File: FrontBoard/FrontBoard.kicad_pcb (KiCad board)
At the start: 2 copper layers, 20.3 x 113.1 mm, 17 parts

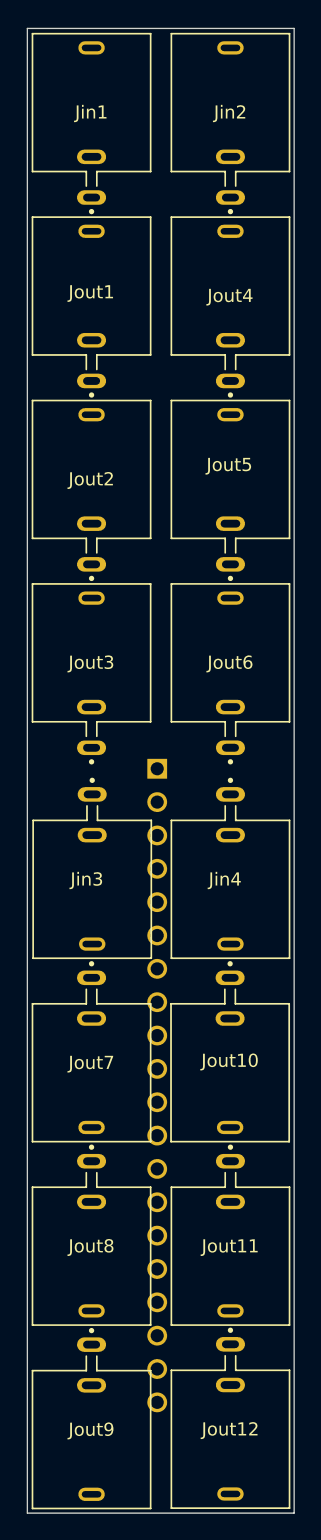
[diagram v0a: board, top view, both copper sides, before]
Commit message: updated with new footprints and 3d models
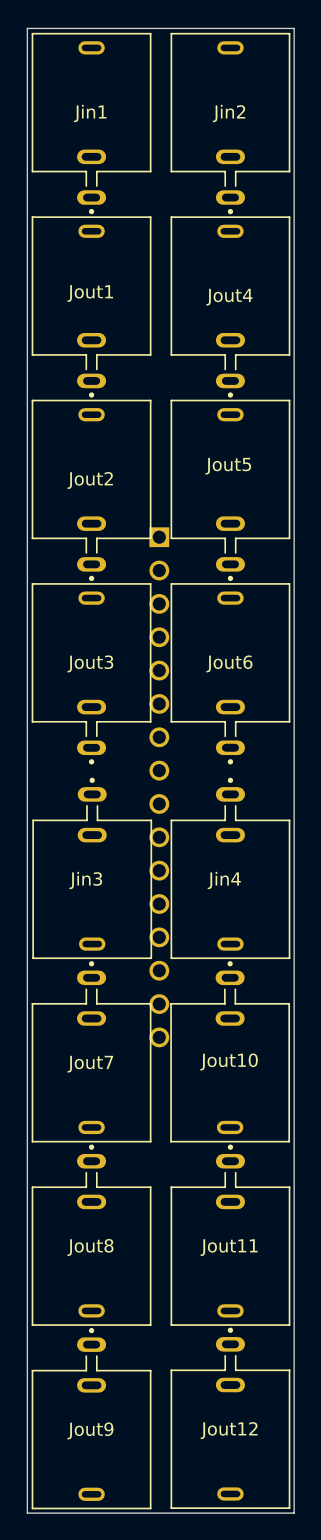
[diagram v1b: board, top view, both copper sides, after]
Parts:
- Jheader1: footprint 2-826646-0:TE_2-826646-0 -> TE_1-826936-6:TE_1-826936-6
- moved Jheader1 22.7 mm to (162.4, 97.1)
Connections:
- Jin1 pad 1: GNDPWR -> GND
- Jin1 pad 2: GNDPWR -> GND
- Jin2 pad 1: GNDPWR -> GND
- Jin3 pad 1: GNDPWR -> GND
- Jin4 pad 1: GNDPWR -> GND
- Jout1 pad 1: GNDPWR -> GND
- Jout1 pad 2: GNDPWR -> GND
- Jout10 pad 1: GNDPWR -> GND
- Jout10 pad 2: GNDPWR -> GND
- Jout10 pad 3: Output10 -> Output8
- Jout11 pad 1: GNDPWR -> GND
- Jout11 pad 2: GNDPWR -> GND
- Jout11 pad 3: Output11 -> Output9
- Jout12 pad 1: GNDPWR -> GND
- Jout12 pad 2: GNDPWR -> GND
- Jout12 pad 3: Output12 -> Output10
- Jout2 pad 1: GNDPWR -> GND
- Jout2 pad 2: GNDPWR -> GND
- Jout3 pad 1: GNDPWR -> GND
- Jout3 pad 2: GNDPWR -> GND
- Jout5 pad 1: GNDPWR -> GND
- Jout5 pad 2: GNDPWR -> GND
- Jout5 pad 3: Output5 -> Output4
- Jout6 pad 1: GNDPWR -> GND
- Jout6 pad 2: GNDPWR -> GND
- Jout6 pad 3: Output6 -> Output5
- Jout7 pad 1: GNDPWR -> GND
- Jout7 pad 2: GNDPWR -> GND
- Jout7 pad 3: Output7 -> Output6
- Jout9 pad 1: GNDPWR -> GND
- Jout9 pad 2: GNDPWR -> GND
- Jout9 pad 3: Output9 -> Output7

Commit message: updated placement
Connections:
- Jheader1 pad 12: Output8 -> Output5
- Jheader1 pad 13: Output9 -> Output8
- Jheader1 pad 14: Output10 -> Output6
- Jheader1 pad 7: Output5 -> Output9
- Jheader1 pad 8: Output6 -> Output10
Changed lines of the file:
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@@
   (footprint "TE_1-826936-6:TE_1-826936-6" (layer "B.Cu")
     (at 162.45 97.12 -90)
-    (property "Comment" "2-826646-0")
+    (property "Centerline_Pitch" "2.54 mm[.1 in]")
+    (property "Comment" "1-826936-6")
     (property "EU_RoHS_Compliance" "Compliant")
+    (property "Number_of_Positions" "16")
+    (property "Product_Type" "Connector")
     (property "Sheetfile" "FrontBoard.kicad_sch")
     (property "Sheetname" "")
+    (property "Sim.Device" "SPICE")
+    (property "Sim.Enable" "0")
+    (property "Sim.Params" "type=\"J\" model=\"2-826646-0\" lib=\"\"")
+    (property "Sim.Pins" "1=1 2=2 3=3 4=4 5=5 6=6 7=7 8=8 9=9 10=10 11=11 12=12 13=13 14=14 15=15 16=16 17=17 18=18 19=19 20=20")
     (attr through_hole)
     (fp_text reference "Jheader1" (at -18.145 2.885 90) (layer "B.SilkS")
@@
       (net 6 "Output4") (pinfunction "6") (pintype "passive"))
     (pad "7" thru_hole circle (at -3.81 0 270) (size 1.508 1.508) (drill 1) (layers "*.Cu" "*.Mask")
-      (net 7 "Output5") (pinfunction "7") (pintype "passive"))
+      (net 12 "Output9") (pinfunction "7") (pintype "passive"))
     (pad "8" thru_hole circle (at -1.27 0 270) (size 1.508 1.508) (drill 1) (layers "*.Cu" "*.Mask")
-      (net 8 "Output6") (pinfunction "8") (pintype "passive"))
+      (net 13 "Output10") (pinfunction "8") (pintype "passive"))
     (pad "9" thru_hole circle (at 1.27 0 270) (size 1.508 1.508) (drill 1) (layers "*.Cu" "*.Mask")
       (net 16 "InputBus3") (pinfunction "9") (pintype "passive"))
@@
       (net 9 "Output7") (pinfunction "11") (pintype "passive"))
     (pad "12" thru_hole circle (at 8.89 0 270) (size 1.508 1.508) (drill 1) (layers "*.Cu" "*.Mask")
-      (net 10 "Output8") (pinfunction "12") (pintype "passive"))
+      (net 7 "Output5") (pinfunction "12") (pintype "passive"))
     (pad "13" thru_hole circle (at 11.43 0 270) (size 1.508 1.508) (drill 1) (layers "*.Cu" "*.Mask")
-      (net 12 "Output9") (pinfunction "13") (pintype "passive"))
+      (net 10 "Output8") (pinfunction "13") (pintype "passive"))
     (pad "14" thru_hole circle (at 13.97 0 270) (size 1.508 1.508) (drill 1) (layers "*.Cu" "*.Mask")
-      (net 13 "Output10") (pinfunction "14") (pintype "passive"))
+      (net 8 "Output6") (pinfunction "14") (pintype "passive"))
     (pad "15" thru_hole circle (at 16.51 0 270) (size 1.508 1.508) (drill 1) (layers "*.Cu" "*.Mask")
       (net 14 "Output11") (pinfunction "15") (pintype "passive"))

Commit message: first pass at routing mainboard
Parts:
- Jheader1: footprint TE_1-826936-6:TE_1-826936-6 -> ESQ-120-12-T-S:SAMTEC_ESQ-120-12-T-S
- moved Jheader1 35.0 mm to (162.5, 62.1)
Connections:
- Jout10 pad 3: Output8 -> Output10
- Jout11 pad 3: Output9 -> Output11
- Jout12 pad 3: Output10 -> Output12
- Jout4 pad 1: GNDPWR -> GND
- Jout4 pad 2: GNDPWR -> GND
- Jout5 pad 3: Output4 -> Output5
- Jout6 pad 3: Output5 -> Output6
- Jout7 pad 3: Output6 -> Output7
- Jout8 pad 1: GNDPWR -> GND
- Jout8 pad 2: GNDPWR -> GND
- Jout9 pad 3: Output7 -> Output9

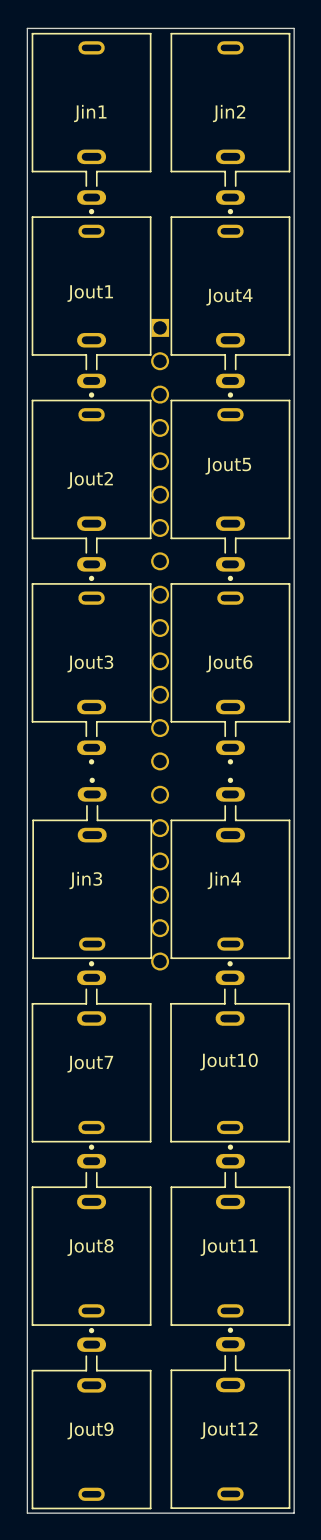
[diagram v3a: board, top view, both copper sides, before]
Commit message: converted MainBoard to 4 layer stackup
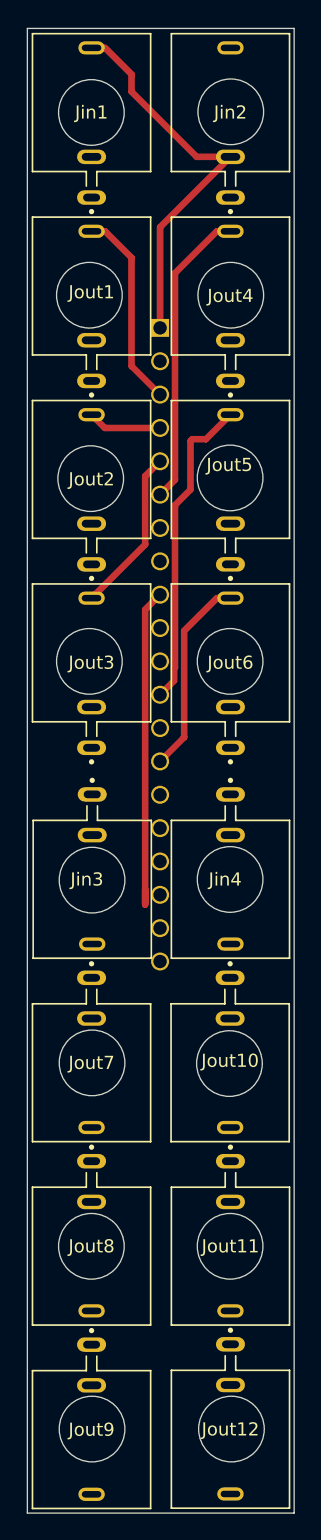
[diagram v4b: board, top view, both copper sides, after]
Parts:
- added REF**: MountingHole_5mm, MountingHole:MountingHole_5mm, B.Cu at (167.8, 118.2)
- added REF**: MountingHole_5mm, MountingHole:MountingHole_5mm, B.Cu at (157.3, 146.0)
- added REF**: MountingHole_5mm, MountingHole:MountingHole_5mm, B.Cu at (157.1, 87.5)
- added REF**: MountingHole_5mm, MountingHole:MountingHole_5mm, B.Cu at (157.3, 132.1)
- added REF**: MountingHole_5mm, MountingHole:MountingHole_5mm, B.Cu at (167.8, 87.5)
- added REF**: MountingHole_5mm, MountingHole:MountingHole_5mm, B.Cu at (167.8, 104.1)
- added REF**: MountingHole_5mm, MountingHole:MountingHole_5mm, B.Cu at (157.2, 73.6)
- added REF**: MountingHole_5mm, MountingHole:MountingHole_5mm, B.Cu at (167.9, 146.0)
- added REF**: MountingHole_5mm, MountingHole:MountingHole_5mm, B.Cu at (157.3, 104.2)
- added REF**: MountingHole_5mm, MountingHole:MountingHole_5mm, B.Cu at (167.9, 45.7)
- added REF**: MountingHole_5mm, MountingHole:MountingHole_5mm, B.Cu at (157.3, 118.1)
- added REF**: MountingHole_5mm, MountingHole:MountingHole_5mm, B.Cu at (167.8, 73.6)
- added REF**: MountingHole_5mm, MountingHole:MountingHole_5mm, B.Cu at (157.3, 45.7)
- added REF**: MountingHole_5mm, MountingHole:MountingHole_5mm, B.Cu at (167.8, 132.1)
- added REF**: MountingHole_5mm, MountingHole:MountingHole_5mm, B.Cu at (167.9, 59.6)
- added REF**: MountingHole_5mm, MountingHole:MountingHole_5mm, B.Cu at (157.1, 59.6)
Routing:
- net InputBus1: track 0.00 -> 30.0 mm
- net InputBus3: track 0.00 -> 25.3 mm
- net Output5: track 0.00 -> 24.2 mm
- net Output4: track 0.00 -> 22.9 mm
- net Output6: track 0.00 -> 15.3 mm
- net Output1: track 0.00 -> 15.2 mm
- net Output3: track 0.00 -> 12.6 mm
- net Output2: track 0.00 -> 5.64 mm

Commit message: WIP: added faceplate
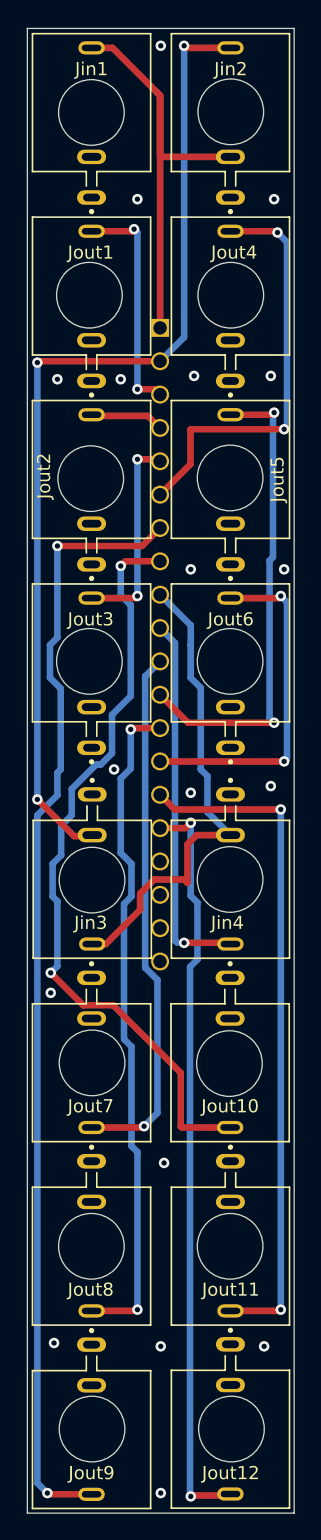
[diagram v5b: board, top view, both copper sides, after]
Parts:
- renumbered REF** to Jinhole1, REF** to Jinhole2, REF** to Jinhole3, REF** to Jinhole4, REF** to Jouthole1, REF** to Jouthole11, REF** to Jouthole3, REF** to Jouthole4, REF** to Jouthole5, REF** to Jouthole7, REF** to Jouthole9, REF** to jouthole10, REF** to jouthole12, REF** to jouthole2, REF** to jouthole6, REF** to jouthole8
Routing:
- net Output9: track 0.00 -> 85.6 mm, vias 0 -> 2
- net InputBus2: track 0.00 -> 76.4 mm, vias 0 -> 3
- net Output10: track 0.00 -> 58.4 mm, vias 0 -> 2
- net Output12: track 0.00 -> 57.4 mm, vias 0 -> 2
- net Output11: track 0.00 -> 51.6 mm, vias 0 -> 2
- net Output8: track 0.00 -> 51.3 mm, vias 0 -> 2
- net Output7: track 0.00 -> 40.7 mm, vias 0 -> 1
- net InputBus4: track 0.00 -> 28.2 mm, vias 0 -> 1
- net Output5: track 24.2 -> 36.9 mm, vias 0 -> 2
- net InputBus3: track 25.3 -> 37.1 mm
- net Output6: track 15.3 -> 25.9 mm, vias 0 -> 2
- net Output4: track 22.9 -> 32.1 mm, vias 0 -> 2
- net InputBus1: track 30.0 -> 34.5 mm
- net Output3: track 12.6 -> 15.8 mm, vias 0 -> 2
- net Output1: track 15.2 -> 17.5 mm, vias 0 -> 2
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- added copper zone on In1.Cu, net GND
- added copper zone on In2.Cu, net GND
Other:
- copper layers 2 -> 4

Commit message: sent to production v1.0.0
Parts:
- moved Jouthole3 0.19 mm to (157.3, 87.6), turned to 0 degrees
- moved Jouthole1 0.17 mm to (157.3, 59.7)
- moved Jouthole5 0.10 mm to (167.9, 73.7)
- moved jouthole6 0.10 mm to (167.9, 87.6), turned to 0 degrees
- moved jouthole2 0.08 mm to (157.3, 73.7), turned to 0 degrees
- moved jouthole12 0.08 mm to (167.9, 146.0)
- moved jouthole10 0.07 mm to (167.8, 118.1)
- moved Jinhole2 0.06 mm to (167.9, 45.7), turned to 0 degrees
- moved Jouthole4 0.06 mm to (167.9, 59.7), turned to 0 degrees
- moved Jinhole3 0.05 mm to (157.3, 104.1)
- turned Jinhole1 to 0 degrees
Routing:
- net Output5: track 36.9 -> 37.5 mm
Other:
- board text added: "R-mods v1.0.0 2023"

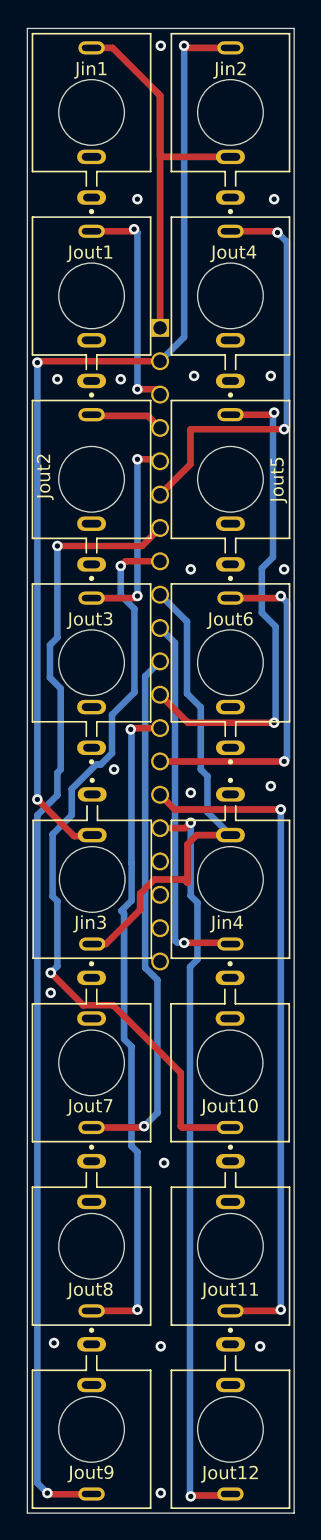
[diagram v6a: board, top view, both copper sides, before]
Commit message: fixed incorrect routing on Jheader1, moved silk screens to back layer for easy readability after assembly, oriented all jacks in the upright postition to solvealignnment descrepency in 3d model vs gerber print
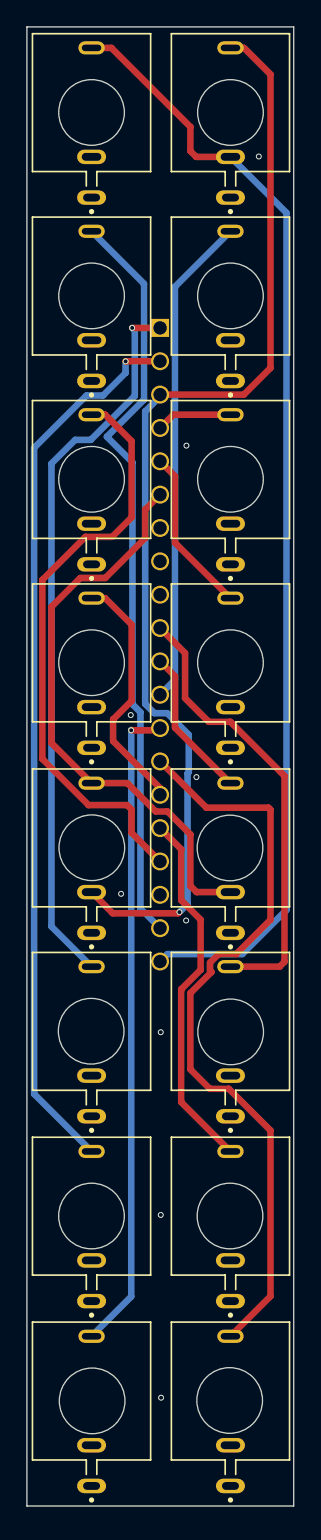
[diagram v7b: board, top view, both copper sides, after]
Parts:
- moved Jin3 2.42 mm to (157.3, 101.7), turned to 0 degrees
- moved Jinhole3 2.42 mm to (157.3, 101.7)
- moved Jin4 2.42 mm to (167.9, 101.7), turned to 0 degrees
- moved Jouthole7 2.41 mm to (157.3, 115.7)
- moved Jout10 2.41 mm to (167.9, 115.7), turned to 0 degrees
- moved Jout7 2.41 mm to (157.3, 115.7), turned to 0 degrees
- moved Jinhole4 2.40 mm to (167.8, 101.7)
- moved jouthole10 2.36 mm to (167.9, 115.7), turned to 0 degrees
- moved Jouthole11 2.31 mm to (167.8, 129.8), turned to 0 degrees
- moved jouthole8 2.31 mm to (157.3, 129.8), turned to 0 degrees
- moved Jout11 2.31 mm to (167.9, 129.8), turned to 0 degrees
- moved Jout8 2.31 mm to (157.3, 129.8), turned to 0 degrees
- moved jouthole12 2.20 mm to (167.8, 143.8), turned to 0 degrees
- moved Jouthole9 2.17 mm to (157.3, 143.9), turned to 0 degrees
- moved Jout12 2.17 mm to (167.9, 143.9), turned to 0 degrees
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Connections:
- Jheader1 pad 01: InputBus1 -> Output7
- Jheader1 pad 02: InputBus2 -> Output8
- Jheader1 pad 03: Output1 -> InputBus2
- Jheader1 pad 04: Output2 -> Output5
- Jheader1 pad 05: Output3 -> Output6
- Jheader1 pad 06: Output4 -> InputBus3
- Jheader1 pad 07: Output9 -> GND
- Jheader1 pad 08: Output10 -> GND
- Jheader1 pad 09: InputBus3 -> GND
- Jheader1 pad 10: InputBus4 -> Output10
- Jheader1 pad 11: Output7 -> InputBus4
- Jheader1 pad 12: Output5 -> Output4
- Jheader1 pad 13: Output8 -> Output9
- Jheader1 pad 14: Output6 -> Output12
- Jheader1 pad 15: Output11 -> Output3
- Jheader1 pad 16: Output12 -> Output11
- Jheader1 pad 17: GND -> Output2
- Jheader1 pad 19: GND -> Output1
- Jheader1 pad 20: GND -> InputBus1
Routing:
- net InputBus1: track 34.5 -> 85.5 mm
- net Output1: track 17.5 -> 57.6 mm, vias 2 -> 0
- net Output2: track 5.64 -> 45.3 mm
- net Output9: track 85.6 -> 49.7 mm, vias 2 -> 1
- net Output5: track 37.5 -> 5.78 mm, vias 2 -> 0
- net Output10: track 58.6 -> 34.6 mm, vias 2 -> 0
- net Output11: track 51.6 -> 28.1 mm, vias 2 -> 0
- net Output8: track 50.9 -> 68.2 mm, vias 2 -> 1
- net InputBus4: track 28.2 -> 11.5 mm, vias 1 -> 0
- net Output7: track 40.7 -> 55.4 mm
- net Output6: track 25.9 -> 12.6 mm, vias 2 -> 0
- net InputBus2: track 76.4 -> 85.0 mm, vias 3 -> 1
- net InputBus3: track 37.1 -> 44.1 mm
- net Output4: track 32.1 -> 37.5 mm, vias 2 -> 0
- net Output3: track 15.8 -> 18.9 mm, vias 2 -> 0
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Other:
- board size 20.3 x 113.1 mm -> 20.3 x 112.7 mm
- board text added: "R-mods v1.0.1 2023"
- board text removed: "R-mods v1.0.0 2023"
